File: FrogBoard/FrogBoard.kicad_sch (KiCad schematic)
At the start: 0 parts

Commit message: 1st draft of schematic
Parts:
- added C1: 10uF, Capacitor_SMD:C_0805_2012Metric_Pad1.18x1.45mm_HandSolder, symbol Device:C
- added C2, C3, C4: 100nF, Capacitor_SMD:C_0603_1608Metric_Pad1.08x0.95mm_HandSolder, symbol Device:C
- added C5: 1uF, Capacitor_SMD:C_0805_2012Metric_Pad1.18x1.45mm_HandSolder, symbol Device:C
- added C6, C7: 1u, Capacitor_SMD:C_0805_2012Metric_Pad1.18x1.45mm_HandSolder, symbol Device:C
- added D1, D2: CUS10S30,H3F, Diode_SMD:D_SOD-323, symbol Diode:MBR0520
- added F1: 1A, Fuse:Fuse_1206_3216Metric_Pad1.42x1.75mm_HandSolder, symbol Device:Fuse
- added FB1: 120R, Resistor_SMD:R_0805_2012Metric_Pad1.20x1.40mm_HandSolder, symbol Device:FerriteBead
- added H1, H4: MountingHole, MountingHole:MountingHole_2.2mm_M2, symbol Mechanical:MountingHole
- added H2, H5: MountingHole, FrogBoard_footprints:MountingHole_1.7mm, symbol Mechanical:MountingHole
- added H3, H6: MountingHole, FrogBoard_footprints:MountingHole_2.833mm, symbol Mechanical:MountingHole
- added J1: Conn_01x10, FrogBoard_footprints:CON_5034801000_MOL, symbol Connector_Generic:Conn_01x10
- added J2: Conn_01x04, symbol Connector_Generic:Conn_01x04
- added J3: USB_B_Micro, Connector_USB:USB_Micro-B_Amphenol_10118193-0001LF_Horizontal, symbol Connector:USB_B_Micro
- added J4: Stickbox, FrogBoard_footprints:Stickbox, symbol FrogBoard:Stickbox
- added R1: 10K, Resistor_SMD:R_0805_2012Metric_Pad1.20x1.40mm_HandSolder, symbol Device:R
- added R2: 100K, Resistor_SMD:R_0805_2012Metric_Pad1.20x1.40mm_HandSolder, symbol Device:R
- added R3, R4: 1k, Resistor_SMD:R_0805_2012Metric_Pad1.20x1.40mm_HandSolder, symbol Device:R
- added U1: STM32L432KBUx, Package_DFN_QFN:QFN-32-1EP_5x5mm_P0.5mm_EP3.45x3.45mm, symbol MCU_ST_STM32L4:STM32L432KBUx
- added U2: USBLC6-2P6, Package_TO_SOT_SMD:SOT-666, symbol Power_Protection:USBLC6-2P6
- added U3: MCP1700T-3302E, Package_TO_SOT_SMD:SOT-23, symbol Regulator_Linear:MCP1700x-330xxTT
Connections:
- new net: R1.1, R2.1, U1.31 (PH3)
- new net: C6.1, F1.2, U3.3 (VI)
- new net +3.3V: C1.2, C2.2, C3.2, C5.2, D1.1 (K), D2.1 (K), FB1.2, R3.1, R4.1, U1.1 (VDD), U1.17 (VDD), U1.4 (NRST)
- new net +3.3VA: C4.2, FB1.1, J4.3 (VCC), U1.5 (VDDA)
- new net +3.3V_HORI: D1.2 (A), J1.7 (Pin_7), J2.4 (Pin_4)
- new net +3.3V_USB: C7.2, D2.2 (A), R1.2, U3.2 (VO)
- new net AX_IN: J4.4 (RAW_X)
- new net AX_OUT: J2.3 (Pin_3), U1.10 (PA4)
- new net AY_IN: J4.5 (RAW_Y)
- new net AY_OUT: J2.2 (Pin_2), U1.11 (PA5)
- new net FFC_P2: J1.2 (Pin_2)
- new net FFC_P3: J1.3 (Pin_3)
- new net FFC_P4: J1.4 (Pin_4)
- new net FFC_P5: J1.5 (Pin_5)
- new net FFC_P6: J1.6 (Pin_6)
- new net GND: C1.1, C2.1, C3.1, C4.1, C5.1, C6.2, C7.1, J1.1 (Pin_1), J1.10 (Pin_10), J2.1 (Pin_1), J3.5 (GND), J4.1 (GND), R2.2, U1.16 (VSS), U1.32 (VSS), U1.33 (VSS), U2.2 (GND), U3.1 (GND)
- new net SCL: J1.9 (Pin_9)
- new net SDA: J1.8 (Pin_8)
- new net STICK_BTN: J4.2 (BTN)
- new net S_SCL: R4.2
- new net S_SDA: R3.2
- new net USB+: U2.4 (I/O2)
- new net USB-: U2.6 (I/O1)
- new net USB_RAW+: J3.3 (D+), U2.3 (I/O2)
- new net USB_RAW-: J3.2 (D-), U2.1 (I/O1)
- new net VBUS: F1.1, J3.1 (VBUS), U2.5 (VBUS)
- no-connect marks 0 -> 11
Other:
- note added: "Connectors"
- note added: "Does this BOOT0 circuit work? I want it to boot into programming mode whenever USB is plugged in."
- note added: "I2C Pullups"
- note added: "MCU"
- note added: "Mounting holes"
- note added: "Note: The assignment of AX/AY to PA4/PA5 is not sensitive"
- note added: "Power"
- note added: "Stickbox"
- note added: "TODO: Should VDDA be connected like this, or just VDD=VDDA? Does it even make sense if the DAC output uses the hori 3.3v as reference?"
- title: (none) -> FrogBoard

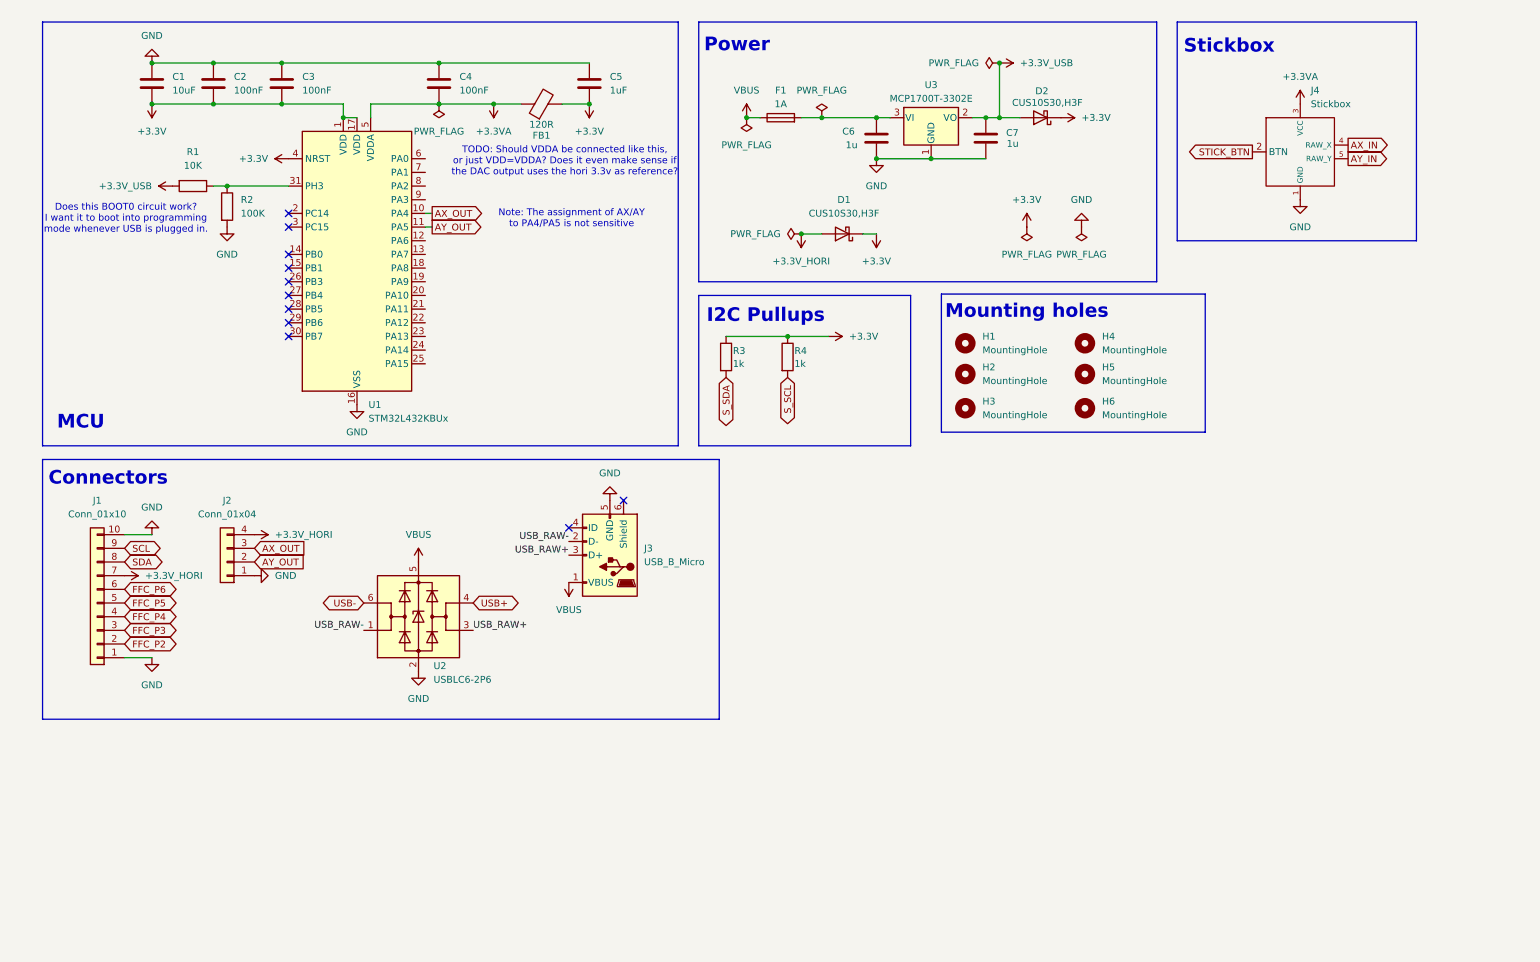
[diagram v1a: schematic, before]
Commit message: PCB outline/initial layout
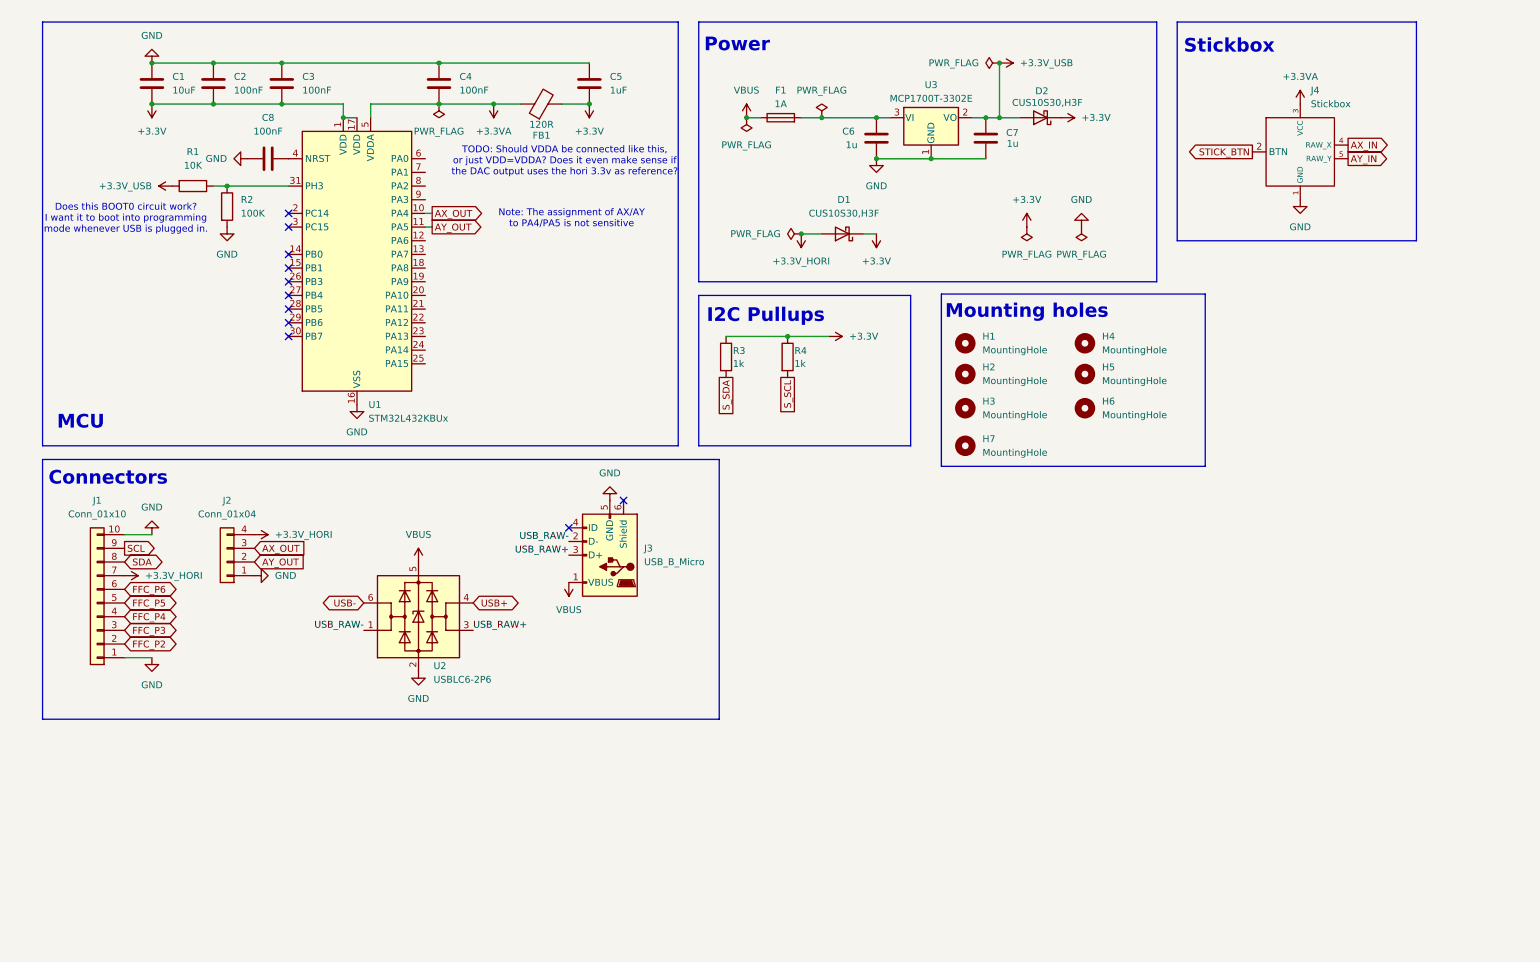
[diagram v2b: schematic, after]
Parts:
- added C8: 100nF, Capacitor_SMD:C_0603_1608Metric_Pad1.08x0.95mm_HandSolder, symbol Device:C
- added H7: MountingHole, MountingHole:MountingHole_4.5mm, symbol Mechanical:MountingHole
- J2: footprint (none) -> FrogBoard_footprints:CONN_528070410_MOL
- J3: footprint Connector_USB:USB_Micro-B_Amphenol_10118193-0001LF_Horizontal -> FrogBoard_footprints:AMPHENOL_10118194-0001LF
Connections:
- net +3.3V: no longer U1.4 (NRST)
- net GND: now also C8.1
- new net: C8.2, U1.4 (NRST)
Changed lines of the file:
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@@
 	(rectangle
 		(start 182.245 65.786)
-		(end 231.267 91.44)
+		(end 231.267 97.79)
 		(stroke
 			(width 0)
@@
 	)
 	(global_label "SCL"
-		(shape bidirectional)
+		(shape output)
 		(at 30.48 113.03 0)
 		(fields_autoplaced yes)
@@
 		)
 		(property "Intersheetrefs" "${INTERSHEET_REFS}"
-			(at 38.0841 113.03 0)
+			(at 36.9728 113.03 0)
 			(effects
 				(font
@@
 	)
 	(global_label "S_SDA"
-		(shape bidirectional)
+		(shape passive)
 		(at 142.24 81.28 270)
 		(fields_autoplaced yes)
@@
 		)
 		(property "Intersheetrefs" "${INTERSHEET_REFS}"
-			(at 142.24 91.1217 90)
+			(at 142.24 88.8991 90)
 			(effects
 				(font
@@
 	)
 	(global_label "S_SCL"
-		(shape bidirectional)
+		(shape passive)
 		(at 153.67 81.28 270)
 		(fields_autoplaced yes)
@@
 		)
 		(property "Intersheetrefs" "${INTERSHEET_REFS}"
-			(at 153.67 91.0612 90)
+			(at 153.67 88.8386 90)
 			(effects
 				(font
@@
 	)
 	(symbol
+		(lib_id "Device:C")
+		(at 57.15 40.64 90)
+		(unit 1)
+		(exclude_from_sim no)
+		(in_bom yes)
+		(on_board yes)
+		(dnp no)
+		(fields_autoplaced yes)
+		(property "Reference" "C8"
+			(at 57.15 33.02 90)
+			(effects
+				(font
+					(size 1.27 1.27)
+				)
+			)
+		)
+		(property "Value" "100nF"
+			(at 57.15 35.56 90)
+			(effects
+				(font
+					(size 1.27 1.27)
+				)
+			)
+		)
+		(property "Footprint" "Capacitor_SMD:C_0603_1608Metric_Pad1.08x0.95mm_HandSolder"
+			(at 60.96 39.6748 0)
+			(effects
+				(font
+					(size 1.27 1.27)
+				)
+				(hide yes)
+			)
+		)
+		(property "Datasheet" "~"
+			(at 57.15 40.64 0)
+			(effects
+				(font
+					(size 1.27 1.27)
+				)
+				(hide yes)
+			)
+		)
+		(property "Description" "Unpolarized capacitor"
+			(at 57.15 40.64 0)
+			(effects
+				(font
+					(size 1.27 1.27)
+				)
+				(hide yes)
+			)
+		)
+		(pin "1"
+		)
+		(pin "2"
+		)
+		(instances
+			(project "FrogBoard"
+				(path "/70a1c624-543f-486d-b6f1-90effc8a6c8b"
+					(reference "C8")
+					(unit 1)
+				)
+			)
+		)
+	)
+	(symbol
 		(lib_id "Device:R")
 		(at 49.53 49.53 0)
@@
 			)
 		)
-		(property "Footprint" ""
+		(property "Footprint" "FrogBoard_footprints:CONN_528070410_MOL"
 			(at 49.53 115.57 0)
 			(effects
@@
 	)
 	(symbol
+		(lib_id "power:GND")
+		(at 53.34 40.64 270)
+		(unit 1)
+		(exclude_from_sim no)
+		(in_bom yes)
+		(on_board yes)
+		(dnp no)
+		(fields_autoplaced yes)
+		(property "Reference" "#PWR028"
+			(at 46.99 40.64 0)
+			(effects
+				(font
+					(size 1.27 1.27)
+				)
+				(hide yes)
+			)
+		)
+		(property "Value" "GND"
+			(at 49.53 40.6399 90)
+			(effects
+				(font
+					(size 1.27 1.27)
+				)
+				(justify right)
+			)
+		)
+		(property "Footprint" ""
+			(at 53.34 40.64 0)
+			(effects
+				(font
+					(size 1.27 1.27)
+				)
+				(hide yes)
+			)
+		)
+		(property "Datasheet" ""
+			(at 53.34 40.64 0)
+			(effects
+				(font
+					(size 1.27 1.27)
+				)
+				(hide yes)
+			)
+		)
+		(property "Description" "Power symbol creates a global label with name \"GND\" , ground"
+			(at 53.34 40.64 0)
+			(effects
+				(font
+					(size 1.27 1.27)
+				)
+				(hide yes)
+			)
+		)
+		(pin "1"
+		)
+		(instances
+			(project "FrogBoard"
+				(path "/70a1c624-543f-486d-b6f1-90effc8a6c8b"
+					(reference "#PWR028")
+					(unit 1)
+				)
+			)
+		)
+	)
+	(symbol
 		(lib_id "power:PWR_FLAG")
 		(at 88.9 30.48 180)
@@
 			)
 		)
-		(property "Footprint" "Connector_USB:USB_Micro-B_Amphenol_10118193-0001LF_Horizontal"
+		(property "Footprint" "FrogBoard_footprints:AMPHENOL_10118194-0001LF"
 			(at 116.84 113.03 0)
 			(effects
@@
 	(symbol
 		(lib_id "power:+3.3V")
-		(at 60.96 40.64 90)
+		(at 39.37 45.72 90)
 		(unit 1)
 		(exclude_from_sim no)
@@
 		(dnp no)
 		(fields_autoplaced yes)
-		(property "Reference" "#PWR028"
-			(at 64.77 40.64 0)
+		(property "Reference" "#PWR06"
+			(at 43.18 45.72 0)
 			(effects
 				(font
@@
 			)
 		)
-		(property "Value" "+3.3V"
-			(at 57.15 40.6399 90)
+		(property "Value" "+3.3V_USB"
+			(at 35.56 45.7199 90)
 			(effects
 				(font
@@
 		)
 		(property "Footprint" ""
-			(at 60.96 40.64 0)
+			(at 39.37 45.72 0)
 			(effects
 				(font
@@
 		)
 		(property "Datasheet" ""
-			(at 60.96 40.64 0)
+			(at 39.37 45.72 0)
 			(effects
 				(font
@@
 		)
 		(property "Description" "Power symbol creates a global label with name \"+3.3V\""
-			(at 60.96 40.64 0)
+			(at 39.37 45.72 0)
 			(effects
 				(font
@@
 			(project "FrogBoard"
 				(path "/70a1c624-543f-486d-b6f1-90effc8a6c8b"
-					(reference "#PWR028")
+					(reference "#PWR06")
 					(unit 1)
 				)
@@
 	)
 	(symbol
-		(lib_id "power:+3.3V")
-		(at 39.37 45.72 90)
+		(lib_id "Mechanical:MountingHole")
+		(at 208.915 80.645 0)
 		(unit 1)
 		(exclude_from_sim no)
-		(in_bom yes)
+		(in_bom no)
 		(on_board yes)
 		(dnp no)
 		(fields_autoplaced yes)
-		(property "Reference" "#PWR06"
-			(at 43.18 45.72 0)
+		(property "Reference" "H5"
+			(at 212.09 79.375 0)
 			(effects
 				(font
 					(size 1.27 1.27)
 				)
-				(hide yes)
+				(justify left)
 			)
 		)
-		(property "Value" "+3.3V_USB"
-			(at 35.56 45.7199 90)
+		(property "Value" "MountingHole"
+			(at 212.09 81.915 0)
 			(effects
 				(font
@@
 			)
 		)
-		(property "Footprint" ""
-			(at 39.37 45.72 0)
+		(property "Footprint" "FrogBoard_footprints:MountingHole_1.7mm"
+			(at 208.915 80.645 0)
 			(effects
 				(font
@@
 			)
 		)
-		(property "Datasheet" ""
-			(at 39.37 45.72 0)
+		(property "Datasheet" "~"
+			(at 208.915 80.645 0)
 			(effects
 				(font
@@
 			)
 		)
-		(property "Description" "Power symbol creates a global label with name \"+3.3V\""
-			(at 39.37 45.72 0)
+		(property "Description" ""
+			(at 208.915 80.645 0)
 			(effects
 				(font
@@
 			)
 		)
-		(pin "1"
+		(property "DIGIKEY" ""
+			(at 208.915 80.645 0)
+			(effects
+				(font
+					(size 1.27 1.27)
+				)
+				(hide yes)
+			)
 		)
 		(instances
 			(project "FrogBoard"
 				(path "/70a1c624-543f-486d-b6f1-90effc8a6c8b"
-					(reference "#PWR06")
+					(reference "H5")
 					(unit 1)
 				)
@@
 	(symbol
 		(lib_id "Mechanical:MountingHole")
-		(at 208.915 80.645 0)
+		(at 186.69 93.98 0)
 		(unit 1)
 		(exclude_from_sim no)
@@
 		(on_board yes)
 		(dnp no)
-		(fields_autoplaced yes)
-		(property "Reference" "H5"
-			(at 212.09 79.375 0)
+		(property "Reference" "H7"
+			(at 189.865 92.71 0)
 			(effects
 				(font
@@
 		)
 		(property "Value" "MountingHole"
-			(at 212.09 81.915 0)
+			(at 189.865 95.25 0)
 			(effects
 				(font
@@
 			)
 		)
-		(property "Footprint" "FrogBoard_footprints:MountingHole_1.7mm"
-			(at 208.915 80.645 0)
+		(property "Footprint" "MountingHole:MountingHole_4.5mm"
+			(at 186.69 93.98 0)
 			(effects
 				(font
@@
 		)
 		(property "Datasheet" "~"
-			(at 208.915 80.645 0)
+			(at 186.69 93.98 0)
 			(effects
 				(font
@@
 		)
 		(property "Description" ""
-			(at 208.915 80.645 0)
+			(at 186.69 93.98 0)
 			(effects
 				(font
@@
 		)
 		(property "DIGIKEY" ""
-			(at 208.915 80.645 0)
+			(at 186.69 93.98 0)
 			(effects
 				(font
@@
 			(project "FrogBoard"
 				(path "/70a1c624-543f-486d-b6f1-90effc8a6c8b"
-					(reference "H5")
+					(reference "H7")
 					(unit 1)
 				)

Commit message: Add mux for analog out lines, cleanup schematic
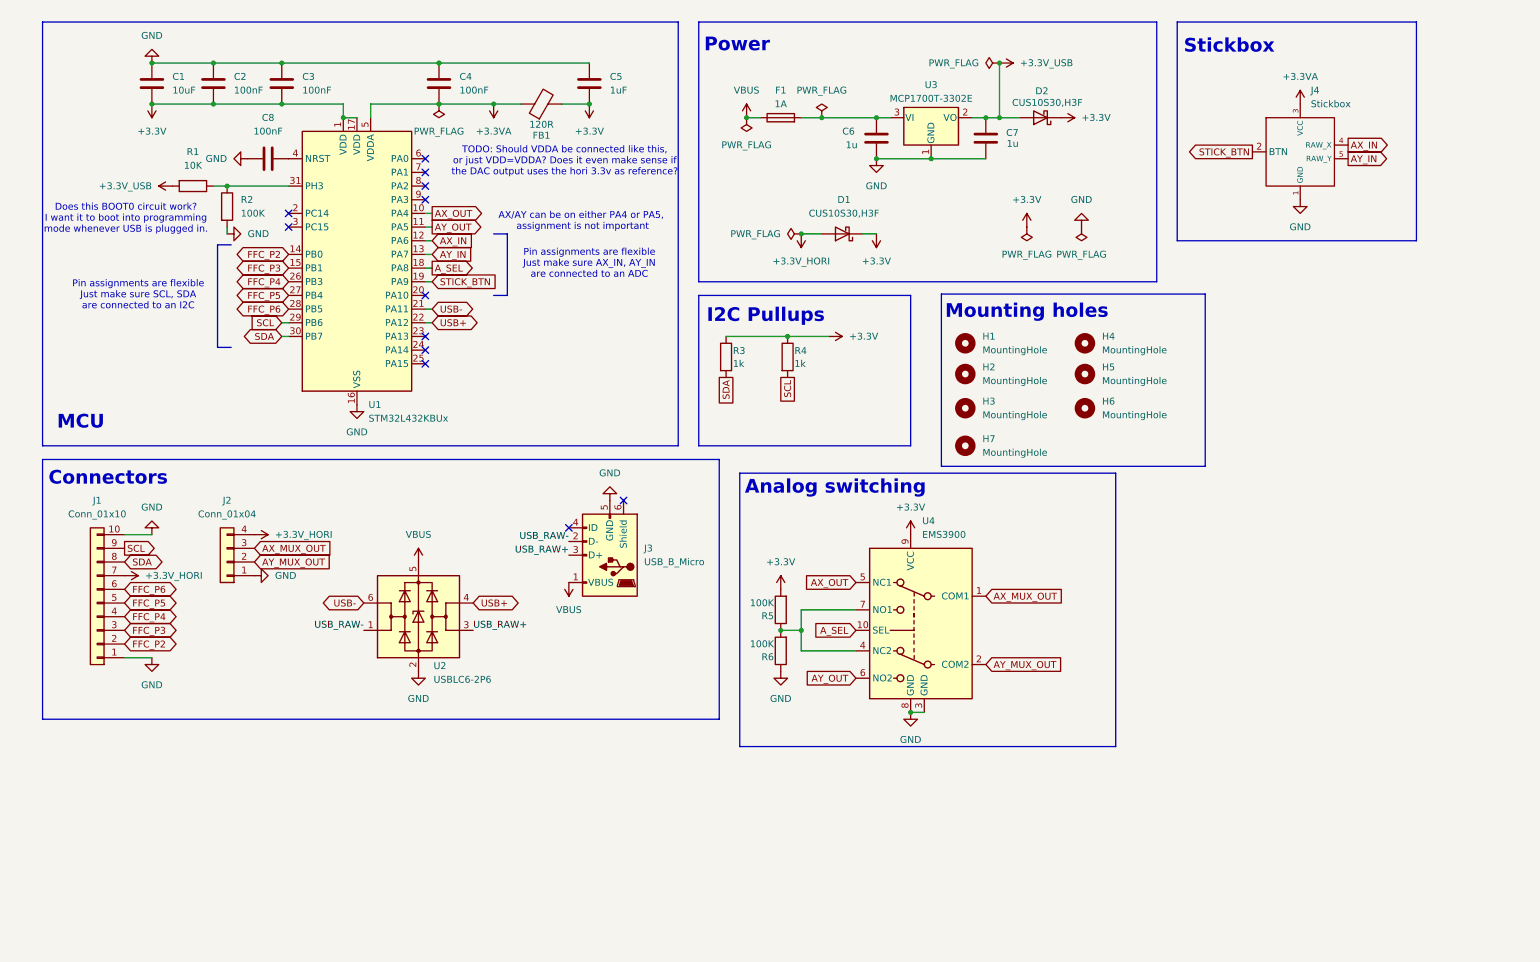
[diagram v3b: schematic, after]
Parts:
- added R5, R6: 100K, Resistor_SMD:R_0603_1608Metric_Pad0.98x0.95mm_HandSolder, symbol Device:R
- added U4: EMS3900, Package_DFN_QFN:UQFN-10_1.4x1.8mm_P0.4mm, symbol FrogBoard:EMS3900
- R1, R2, R3, R4: footprint Resistor_SMD:R_0805_2012Metric_Pad1.20x1.40mm_HandSolder -> Resistor_SMD:R_0603_1608Metric_Pad0.98x0.95mm_HandSolder
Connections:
- net S_SCL is gone; now on net SCL: R4.2
- net S_SDA is gone; now on net SDA: R3.2
- net +3.3V: now also R5.2, U4.9 (VCC)
- net AX_IN: now also U1.12 (PA6)
- net AX_OUT: now also U4.5 (NC1); no longer J2.3 (Pin_3)
- net AY_IN: now also U1.13 (PA7)
- net AY_OUT: now also U4.6 (NO2); no longer J2.2 (Pin_2)
- net FFC_P2: now also U1.14 (PB0)
- net FFC_P3: now also U1.15 (PB1)
- net FFC_P4: now also U1.26 (PB3)
- net FFC_P5: now also U1.27 (PB4)
- net FFC_P6: now also U1.28 (PB5)
- net GND: now also R6.1, U4.11 (GND), U4.3 (GND), U4.8 (GND)
- net SCL: now also U1.29 (PB6)
- net SDA: now also U1.30 (PB7)
- net STICK_BTN: now also U1.19 (PA9)
- net USB+: now also U1.22 (PA12)
- net USB-: now also U1.21 (PA11)
- net A_SEL: now reaches U1.18 (PA8)
- net A_SEL: now also U4.10 (SEL)
- new net: R5.1, R6.2, U4.4 (NC2), U4.7 (NO1)
- new net AX_MUX_OUT: J2.3 (Pin_3), U4.1 (COM1)
- new net AY_MUX_OUT: J2.2 (Pin_2), U4.2 (COM2)
- no-connect marks 11 -> 12
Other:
- note added: "AX/AY can be on either PA4 or PA5, assignment is not important"
- note added: "Pin assignments are flexible Just make sure AX_IN, AY_IN are connected to an ADC"
- note added: "Pin assignments are flexible Just make sure SCL, SDA are connected to an I2C"
- note removed: "Note: The assignment of AX/AY to PA4/PA5 is not sensitive"
